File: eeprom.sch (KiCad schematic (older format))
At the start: 7 parts

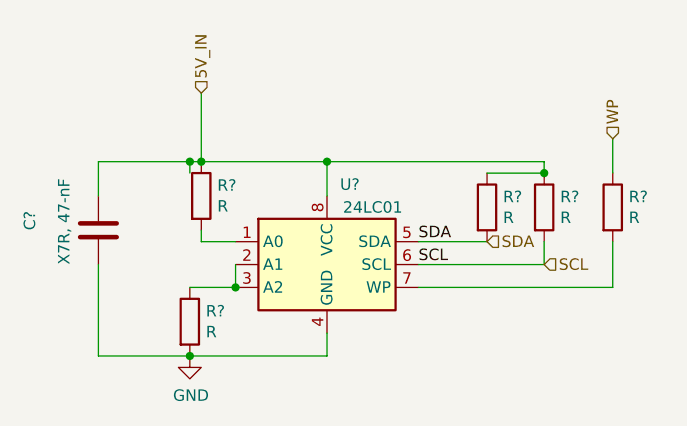
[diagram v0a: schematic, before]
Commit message: update pcb layout
set board cutout
update eeprom footporint
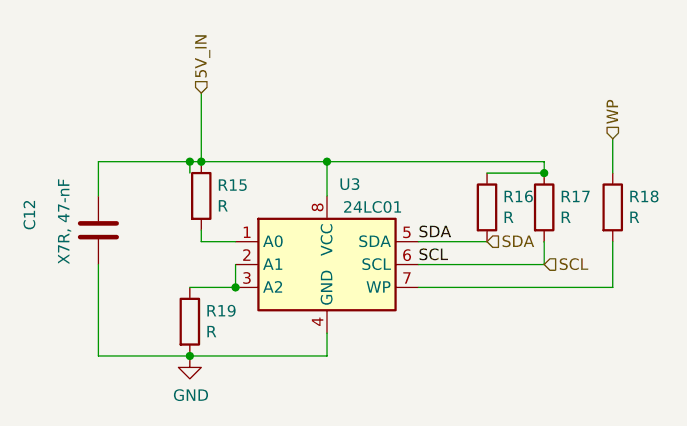
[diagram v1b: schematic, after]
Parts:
- U3: renamed from U?; footprint Package_DFN_QFN:DFN-8-1EP_2x3mm_P0.5mm_EP0.61x2.2mm -> Package_DFN_QFN:DFN-8-1EP_3x2mm_P0.5mm_EP1.36x1.46mm
- gave numbers to parts that had none: 6
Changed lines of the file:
@@
 U 1 1 60F67DC6
 P 4310 3200
-F 0 "U?" H 4410 3550 50  0000 C CNN
+AR Path="/60E74488/60F67DC6" Ref="U?"  Part="1"
+AR Path="/60F66E2D/60F67DC6" Ref="U3"  Part="1"
+F 0 "U3" H 4410 3550 50  0000 C CNN
 F 1 "24LC01" H 4510 3450 50  0000 C CNN
-F 2 "Package_DFN_QFN:DFN-8-1EP_2x3mm_P0.5mm_EP0.61x2.2mm" H 4310 3200 50  0001 C CNN
+F 2 "Package_DFN_QFN:DFN-8-1EP_3x2mm_P0.5mm_EP1.36x1.46mm" H 4310 3200 50  0001 C CNN
 F 3 "http://ww1.microchip.com/downloads/en/DeviceDoc/21711J.pdf" H 4310 3200 50  0001 C CNN
 	1    4310 3200
@@
 U 1 1 60F67DCC
 P 3760 2900
-F 0 "R?" H 3830 2946 50  0000 L CNN
+AR Path="/60E74488/60F67DCC" Ref="R?"  Part="1"
+AR Path="/60F66E2D/60F67DCC" Ref="R15"  Part="1"
+F 0 "R15" H 3830 2946 50  0000 L CNN
 F 1 "R" H 3830 2855 50  0000 L CNN
 F 2 "Resistor_SMD:R_0603_1608Metric_Pad1.05x0.95mm_HandSolder" V 3690 2900 50  0001 C CNN
@@
 U 1 1 60F67DD8
 P 3710 3450
-F 0 "R?" H 3780 3496 50  0000 L CNN
+AR Path="/60E74488/60F67DD8" Ref="R?"  Part="1"
+AR Path="/60F66E2D/60F67DD8" Ref="R19"  Part="1"
+F 0 "R19" H 3780 3496 50  0000 L CNN
 F 1 "R" H 3780 3405 50  0000 L CNN
 F 2 "Resistor_SMD:R_0603_1608Metric_Pad1.05x0.95mm_HandSolder" V 3640 3450 50  0001 C CNN
@@
 U 1 1 60F67DDE
 P 3710 3600
-F 0 "#PWR?" H 3710 3350 50  0001 C CNN
+AR Path="/60E74488/60F67DDE" Ref="#PWR?"  Part="1"
+AR Path="/60F66E2D/60F67DDE" Ref="#PWR0102"  Part="1"
+F 0 "#PWR0102" H 3710 3350 50  0001 C CNN
 F 1 "GND" H 3715 3427 50  0000 C CNN
 F 2 "" H 3710 3600 50  0001 C CNN
@@
 U 1 1 60F67DE4
 P 5010 2950
-F 0 "R?" H 5080 2996 50  0000 L CNN
+AR Path="/60E74488/60F67DE4" Ref="R?"  Part="1"
+AR Path="/60F66E2D/60F67DE4" Ref="R16"  Part="1"
+F 0 "R16" H 5080 2996 50  0000 L CNN
 F 1 "R" H 5080 2905 50  0000 L CNN
 F 2 "Resistor_SMD:R_0603_1608Metric_Pad1.05x0.95mm_HandSolder" V 4940 2950 50  0001 C CNN
@@
 U 1 1 60F67DEA
 P 5260 2950
-F 0 "R?" H 5330 2996 50  0000 L CNN
+AR Path="/60E74488/60F67DEA" Ref="R?"  Part="1"
+AR Path="/60F66E2D/60F67DEA" Ref="R17"  Part="1"
+F 0 "R17" H 5330 2996 50  0000 L CNN
 F 1 "R" H 5330 2905 50  0000 L CNN
 F 2 "Resistor_SMD:R_0603_1608Metric_Pad1.05x0.95mm_HandSolder" V 5190 2950 50  0001 C CNN
@@
 U 1 1 60F67DF8
 P 3310 3050
-F 0 "C?" V 3010 3050 50  0000 L CNN
+AR Path="/60E74488/60F67DF8" Ref="C?"  Part="1"
+AR Path="/60F66E2D/60F67DF8" Ref="C12"  Part="1"
+F 0 "C12" V 3010 3050 50  0000 L CNN
 F 1 "X7R, 47-nF" V 3160 2900 50  0000 L CNN
 F 2 "Capacitor_SMD:C_0603_1608Metric_Pad1.05x0.95mm_HandSolder" H 3348 2900 50  0001 C CNN
@@
 U 1 1 60F67E0E
 P 5560 2950
-F 0 "R?" H 5630 2996 50  0000 L CNN
+AR Path="/60E74488/60F67E0E" Ref="R?"  Part="1"
+AR Path="/60F66E2D/60F67E0E" Ref="R18"  Part="1"
+F 0 "R18" H 5630 2996 50  0000 L CNN
 F 1 "R" H 5630 2905 50  0000 L CNN
 F 2 "Resistor_SMD:R_0603_1608Metric_Pad1.05x0.95mm_HandSolder" V 5490 2950 50  0001 C CNN
